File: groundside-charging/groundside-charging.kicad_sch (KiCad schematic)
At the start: 30 parts, among them J2 Charge Current Out (to Rocket), J3 Charge Voltage Sensing, J4 12V In, Q1 BSS138PW,115, Q2 SI4143DY-T1-GE3, Q3 SI4840BDY-T1-GE3, U1 LM317DCYR, U2 LM3478MA

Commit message: reannotated
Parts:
- removed Q1: BSS138PW,115, Package_TO_SOT_SMD:SOT-323_SC-70_Handsoldering, symbol Device:Q_NMOS_GSD
- removed Q2: SI4143DY-T1-GE3, groundside-charging:SOIC_3DY-T1-GE3_VIS, symbol Device:Q_PMOS_SGD
- removed R1: 120R, Resistor_SMD:R_0805_2012Metric_Pad1.20x1.40mm_HandSolder, symbol Device:R_US
- removed R2, R4: 10k, Resistor_SMD:R_0805_2012Metric_Pad1.20x1.40mm_HandSolder, symbol Device:R_US
- renumbered J4 to J1, Q3 to Q1, R3 to R1, R5 to R2, R6 to R3, R7 to R4, R8 to R5, R9 to R6, R10 to R7, R11 to R8, R12 to R9
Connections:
- net +12V_SW is gone; now on net +12V: C2.1, C3.1, C4.1, L1.1, U2.8 (V_{IN})
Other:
- note removed: "Charge Current Output Enable"
- moved on the sheet: R3

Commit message: layout and routing
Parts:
- added H1, H2, H3, H4: MountingHole, MountingHole:MountingHole_3.2mm_M3_Pad_Via, symbol Mechanical:MountingHole_Pad
- R8, R9: footprint (none) -> Resistor_SMD:R_0805_2012Metric_Pad1.20x1.40mm_HandSolder
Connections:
- net GND: now also J3.2 (Pin_2), R9.2, H1.1, H2.1, H3.1, H4.1
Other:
- moved on the sheet: C1, C2, C3, C4, C5, C6, C7, C8, D1, J1, J2, J3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

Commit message: address tessa feedback
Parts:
- C2, C3: value 68uF -> 68u
- C4: value 100nF -> 100n
- C5: value 820pF -> 820p
- C6: value 15nF -> 15n
- C7: value 10pF -> 10p
- Q1: footprint groundside-charging:SO-8-SINGLE_MS-012_VIS -> groundside-charging:SI4840BDY-T1-GE3
- R5: value 10mR -> 15m
- U1: footprint Package_TO_SOT_SMD:SOT-223-3_TabPin2 -> groundside-charging:LM317DCYR
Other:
- note added: "Based on 8.3.7"
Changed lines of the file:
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@@
 	)
 	(rectangle
-		(start 64.135 82.55)
+		(start 64.135 84.455)
 		(end 111.125 92.075)
 		(stroke
@@
 		)
 	)
+	(text "Based on 8.3.7"
+		(exclude_from_sim no)
+		(at 80.01 173.355 0)
+		(effects
+			(font
+				(size 1.27 1.27)
+			)
+		)
+	)
 	(text "TCJD686M020R0055"
 		(exclude_from_sim no)
@@
 		(fields_autoplaced yes)
 		(property "Reference" "C6"
-			(at 151.765 98.4249 0)
+			(at 152.4 98.4249 0)
 			(effects
 				(font
@@
 			)
 		)
-		(property "Value" "15nF"
-			(at 151.765 100.9649 0)
+		(property "Value" "15n"
+			(at 152.4 100.9649 0)
 			(effects
 				(font
@@
 			)
 		)
-		(property "Value" "100nF"
+		(property "Value" "100n"
 			(at 118.11 89.5349 0)
 			(effects
@@
 			)
 		)
-		(property "Footprint" "groundside-charging:SO-8-SINGLE_MS-012_VIS"
+		(property "Footprint" "groundside-charging:SI4840BDY-T1-GE3"
 			(at 199.39 78.74 0)
 			(effects
@@
 		(fields_autoplaced yes)
 		(property "Reference" "R5"
-			(at 198.755 109.8549 0)
+			(at 199.39 109.8549 0)
 			(effects
 				(font
@@
 			)
 		)
-		(property "Value" "10mR"
-			(at 198.755 112.3949 0)
+		(property "Value" "15m"
+			(at 199.39 112.3949 0)
 			(effects
 				(font
@@
 			)
 		)
-		(property "Footprint" "Package_TO_SOT_SMD:SOT-223-3_TabPin2"
+		(property "Footprint" "groundside-charging:LM317DCYR"
 			(at 80.01 144.145 0)
 			(effects
@@
 			)
 		)
-		(property "Value" "820pF"
+		(property "Value" "820p"
 			(at 139.7 109.2199 0)
 			(effects
@@
 		(fields_autoplaced yes)
 		(property "Reference" "C7"
-			(at 187.325 109.8549 0)
+			(at 187.96 109.8549 0)
 			(effects
 				(font
@@
 			)
 		)
-		(property "Value" "10pF"
-			(at 187.325 112.3949 0)
+		(property "Value" "10p"
+			(at 187.96 112.3949 0)
 			(effects
 				(font
@@
 			)
 		)
-		(property "Datasheet" "~"
+		(property "Datasheet" "https://content.kemet.com/datasheets/KEM_T2076_T52X-530.pdf"
 			(at 224.79 81.28 0)
 			(effects
@@
 		(on_board yes)
 		(dnp no)
-		(fields_autoplaced yes)
 		(property "Reference" "C3"
-			(at 106.045 86.1059 0)
+			(at 105.41 86.995 0)
 			(effects
 				(font
@@
 			)
 		)
-		(property "Value" "68uF"
-			(at 106.045 88.6459 0)
+		(property "Value" "68u"
+			(at 105.41 89.535 0)
 			(effects
 				(font
@@
 		(on_board yes)
 		(dnp no)
-		(fields_autoplaced yes)
 		(property "Reference" "C2"
-			(at 93.345 86.1059 0)
+			(at 92.71 86.995 0)
 			(effects
 				(font
@@
 			)
 		)
-		(property "Value" "68uF"
-			(at 93.345 88.6459 0)
+		(property "Value" "68u"
+			(at 92.71 89.535 0)
 			(effects
 				(font

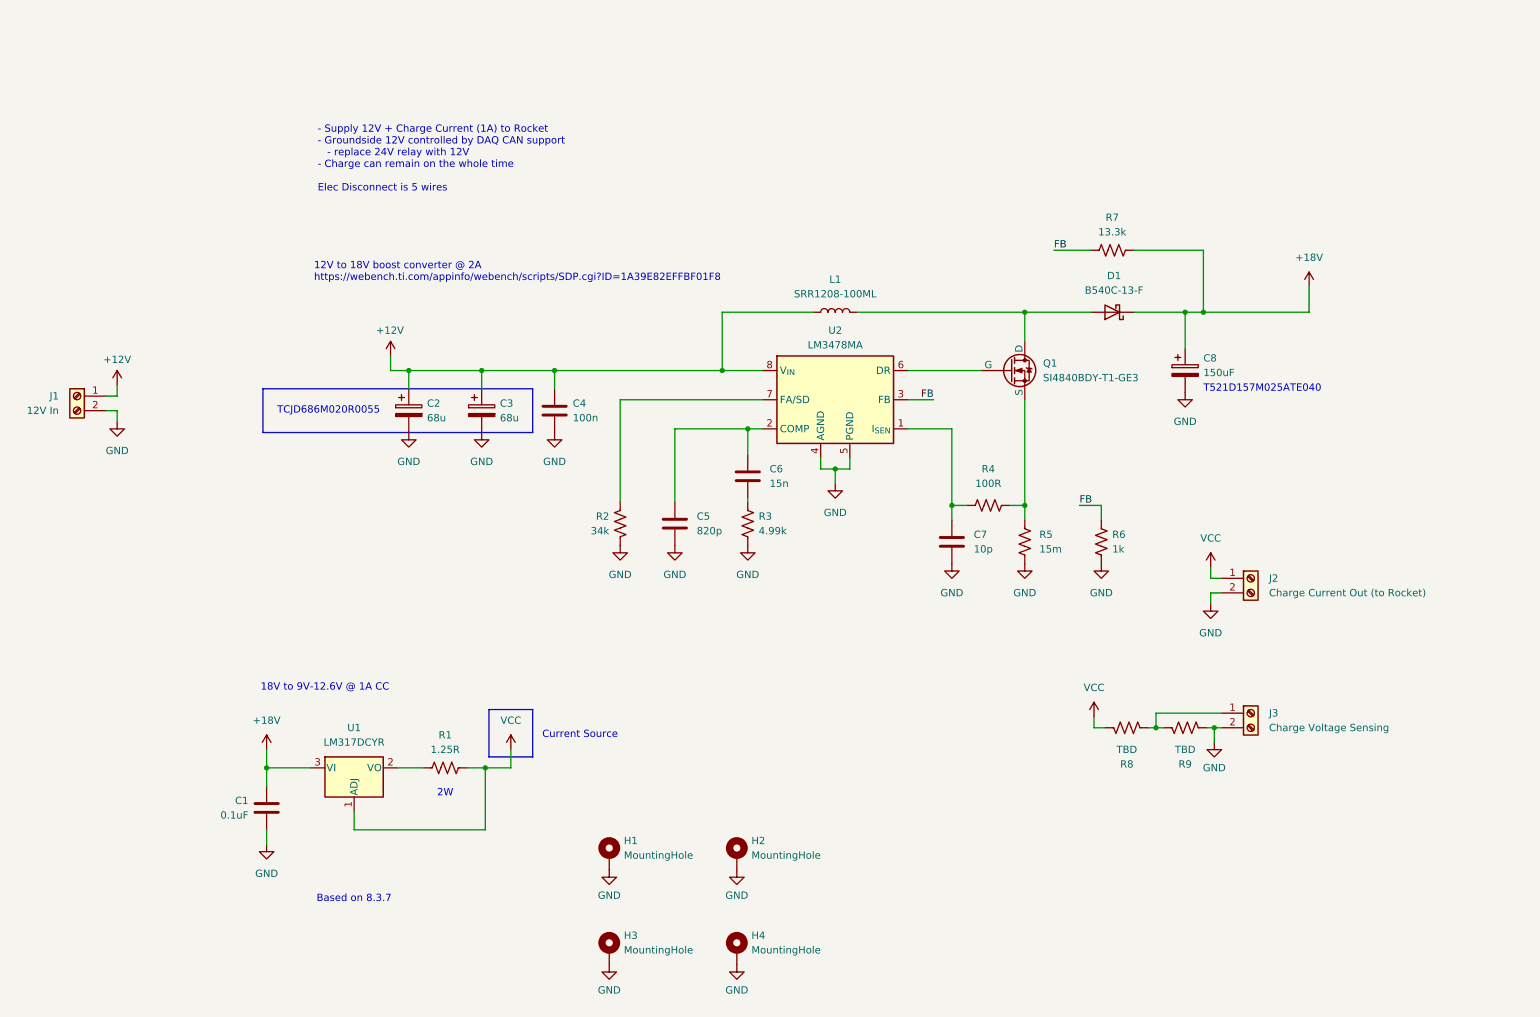
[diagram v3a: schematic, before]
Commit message: change CC source to CC/CV battery charge IC
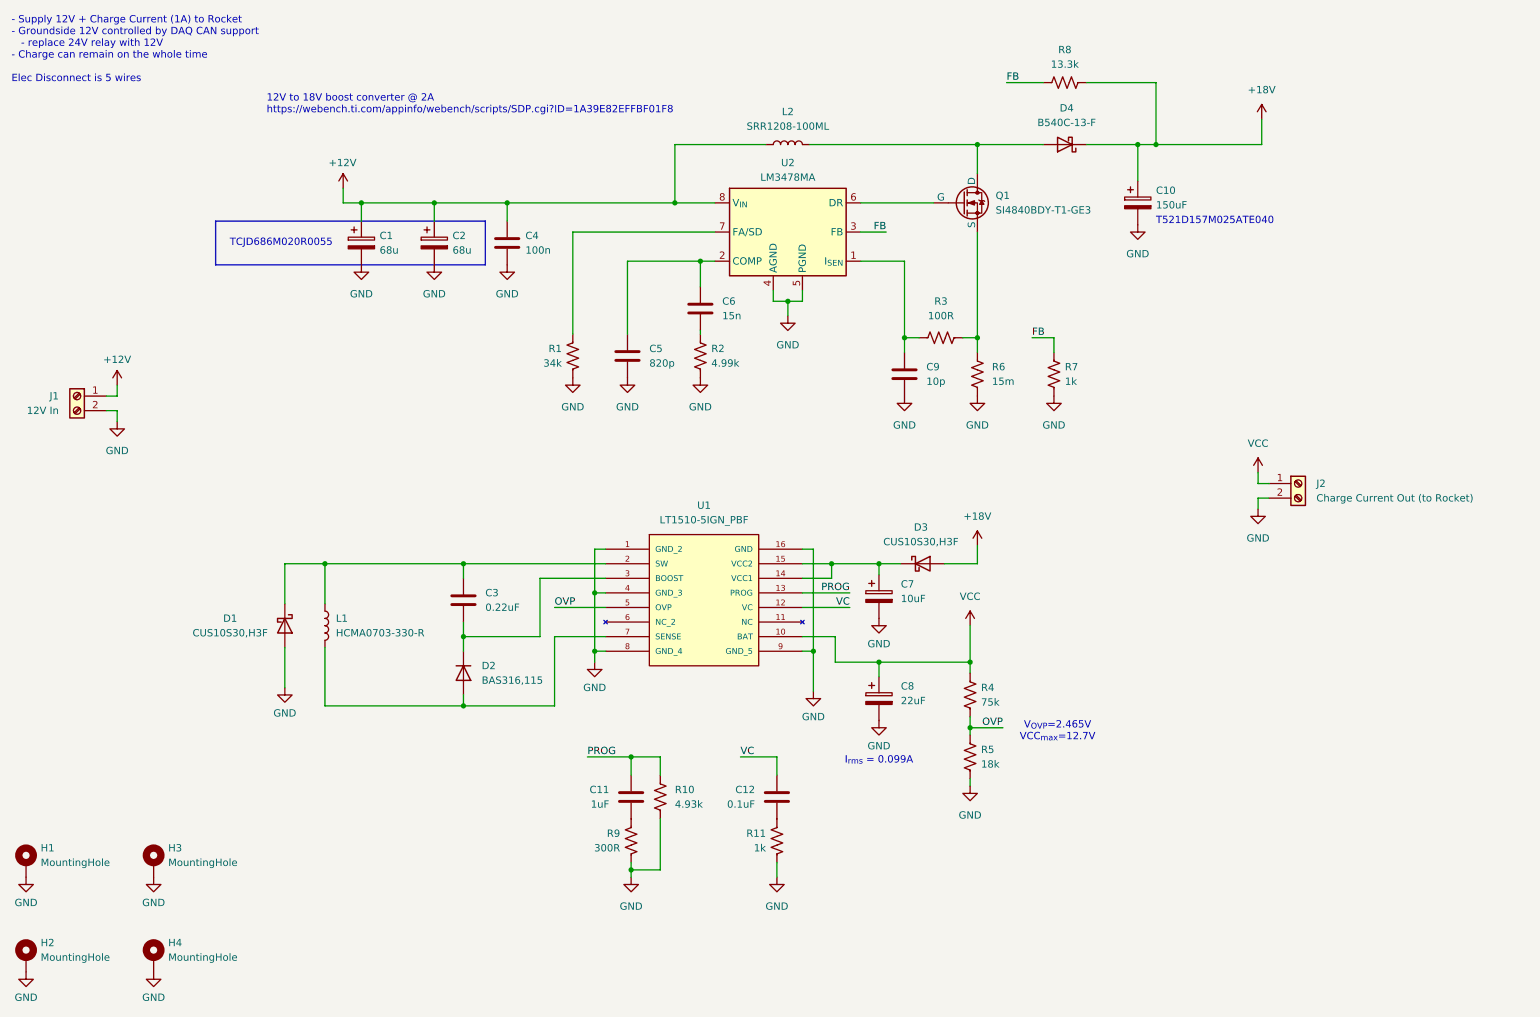
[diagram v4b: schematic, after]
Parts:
- removed C1: 0.1uF, Capacitor_SMD:C_0805_2012Metric_Pad1.18x1.45mm_HandSolder, symbol Device:C
- removed J3: Charge Voltage Sensing, TerminalBlock_Phoenix:TerminalBlock_Phoenix_PT-1,5-2-5.0-H_1x02_P5.00mm_Horizontal, symbol Connector:Screw_Terminal_01x02
- removed R1: 1.25R, Resistor_SMD:R_2512_6332Metric_Pad1.40x3.35mm_HandSolder, symbol Device:R_US
- removed R8: TBD, Resistor_SMD:R_0805_2012Metric_Pad1.20x1.40mm_HandSolder, symbol Device:R_US
- removed U1: LM317DCYR, groundside-charging:LM317DCYR, symbol Regulator_Linear:LM317_SOT-223
- added C11: 1uF, Capacitor_SMD:C_0805_2012Metric_Pad1.18x1.45mm_HandSolder, symbol Device:C
- added C12: 0.1uF, Capacitor_SMD:C_0805_2012Metric_Pad1.18x1.45mm_HandSolder, symbol Device:C
- added C3: 0.22uF, Capacitor_SMD:C_0805_2012Metric_Pad1.18x1.45mm_HandSolder, symbol Device:C
- added C7: 10uF, Capacitor_SMD:C_0805_2012Metric_Pad1.18x1.45mm_HandSolder, symbol Device:C_Polarized
- added C8: 22uF, Capacitor_SMD:C_0805_2012Metric_Pad1.18x1.45mm_HandSolder, symbol Device:C_Polarized
- added D1, D3: CUS10S30,H3F, Diode_SMD:D_SOD-323_HandSoldering, symbol Device:D_Schottky
- added D2: BAS316,115, Diode_SMD:D_SOD-323_HandSoldering, symbol Device:D
- added L1: HCMA0703-330-R, symbol Device:L
- added R10: 4.93k, Resistor_SMD:R_0805_2012Metric_Pad1.20x1.40mm_HandSolder, symbol Device:R_US
- added R11: 1k, Resistor_SMD:R_0805_2012Metric_Pad1.20x1.40mm_HandSolder, symbol Device:R_US
- added R4: 75k, Resistor_SMD:R_0805_2012Metric_Pad1.20x1.40mm_HandSolder, symbol Device:R_US
- added R5: 18k, Resistor_SMD:R_0805_2012Metric_Pad1.20x1.40mm_HandSolder, symbol Device:R_US
- added U1: LT1510-5IGN_PBF, LT1510-5IGN_PBF:SSOP-16_GN, symbol groundside-charging:LT1510-5IGN_PBF
- R9: value TBD -> 300R
- renumbered C2 to C1, C8 to C10, C3 to C2, C7 to C9, D1 to D4, H3 to H2, H2 to H3, L1 to L2, R2 to R1, R3 to R2, R4 to R3, R5 to R6, R6 to R7, R7 to R8
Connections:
- net +18V: now also D3.2 (A)
- net GND: now also C7.2, C8.2, D1.2 (A), R10.2, R11.2, R5.2, U1.1 (GND_2), U1.16 (GND), U1.4 (GND_3), U1.8 (GND_4), U1.9 (GND_5)
- net VCC: now also C8.1, R4.1, U1.10 (BAT)
- net at R9.1: now also C11.2
- new net: C7.1, D3.1 (K), U1.14 (VCC1), U1.15 (VCC2)
- new net: C12.2, R11.1
- new net: C3.1, D1.1 (K), L1.1, U1.2 (SW)
- new net: D2.2 (A), L1.2, U1.7 (SENSE)
- new net: C3.2, D2.1 (K), U1.3 (BOOST)
- new net OVP: R4.2, R5.1, U1.5 (OVP)
- new net PROG: C11.1, R10.1, U1.13 (PROG)
- new net VC: C12.1, U1.12 (VC)
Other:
- note added: "I_{rms} = 0.099A"
- note added: "V_{OVP}=2.465V VCC_{max}=12.7V"
- note removed: "18V to 9V-12.6V @ 1A CC"
- note removed: "2W"
- note removed: "Based on 8.3.7"
- note removed: "Current Source"
- moved on the sheet: C1, C10, C2, C4, C5, C6, C9, D4, H1, H2, H3, H4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

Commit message: select components and layout/route
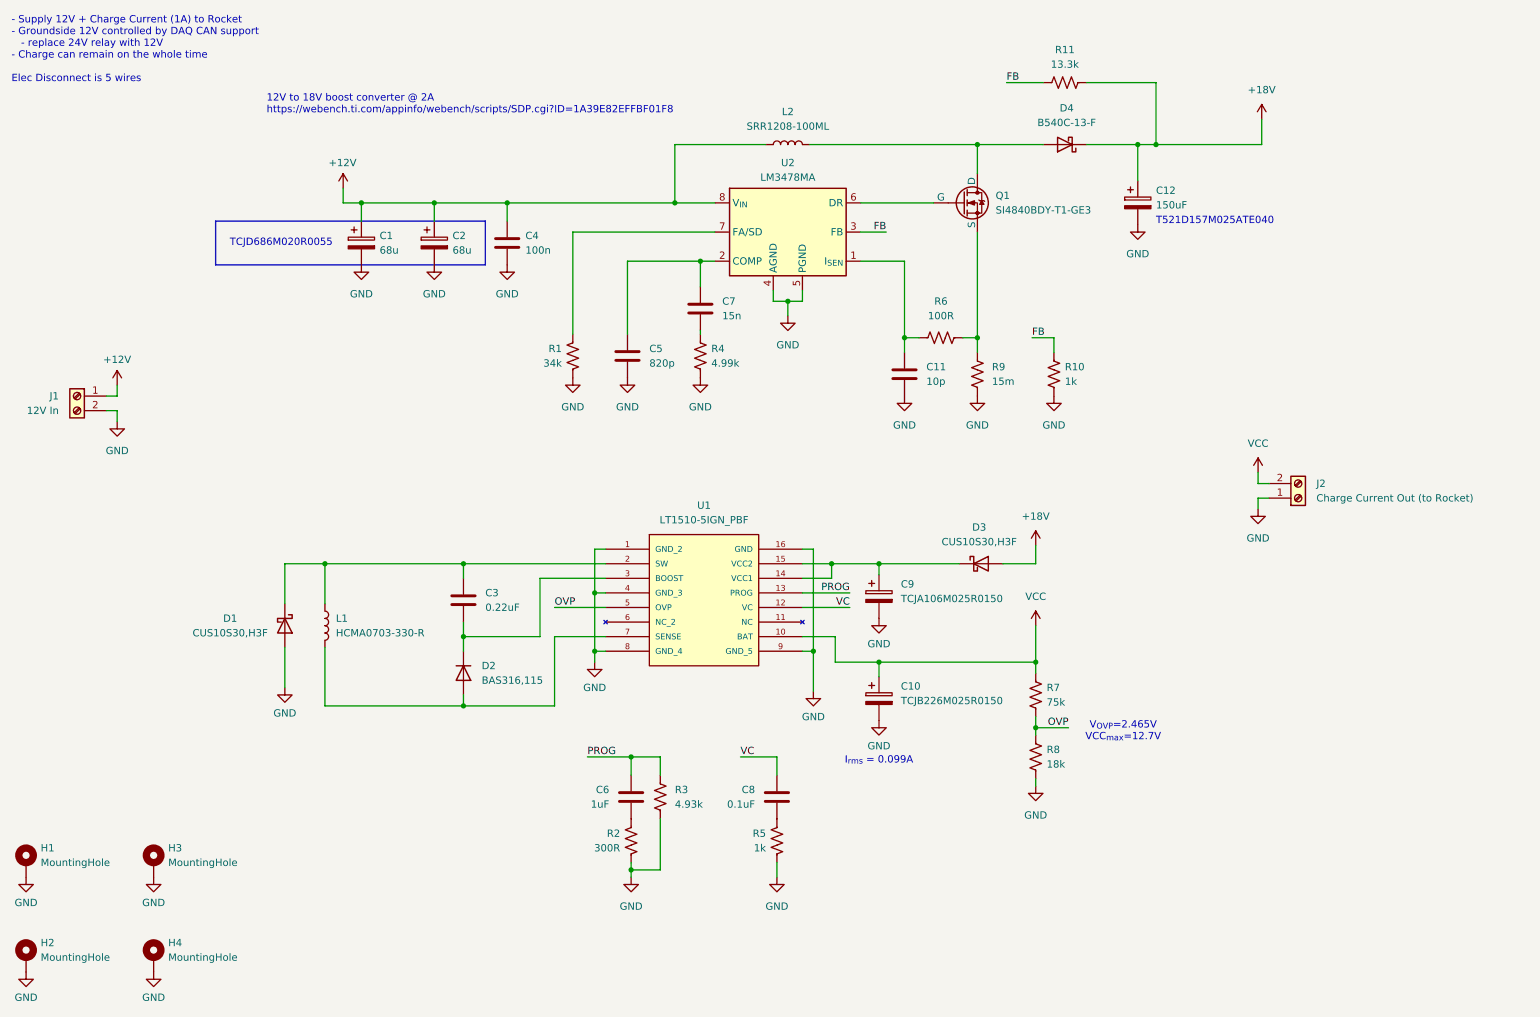
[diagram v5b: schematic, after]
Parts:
- C10: renamed from C8; value 22uF -> TCJB226M025R0150; footprint Capacitor_SMD:C_0805_2012Metric_Pad1.18x1.45mm_HandSolder -> groundside-charging:CAPPM7343X310N
- C9: renamed from C7; value 10uF -> TCJA106M025R0150; footprint Capacitor_SMD:C_0805_2012Metric_Pad1.18x1.45mm_HandSolder -> groundside-charging:CAPPM3216X180N
- L1: footprint (none) -> groundside-charging:HCMA0703-330-R
- U1: footprint LT1510-5IGN_PBF:SSOP-16_GN -> groundside-charging:SSOP-16_GN
- renumbered C9 to C11, C10 to C12, C11 to C6, C6 to C7, C12 to C8, R7 to R10, R8 to R11, R9 to R2, R10 to R3, R2 to R4, R11 to R5, R3 to R6, R4 to R7, R5 to R8, R6 to R9
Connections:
- net GND: now also J2.1 (Pin_1); no longer J2.2 (Pin_2)
- net VCC: now also J2.2 (Pin_2); no longer J2.1 (Pin_1)
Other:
- moved on the sheet: D3, R7, R8
